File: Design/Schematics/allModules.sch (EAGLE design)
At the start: 152 parts, among them IC1 MAX7219CNG, IC2 MAX7219CNG, IC3 MAX7219CNG, IC4 MAX7219CNG, SW1 arcade_btn, SW2 arcade_btn, SW3 arcade_btn, SW4 arcade_btn, U1 328P, U2 328P, U3 328P, U4 328P, U5 328P, U6 328P

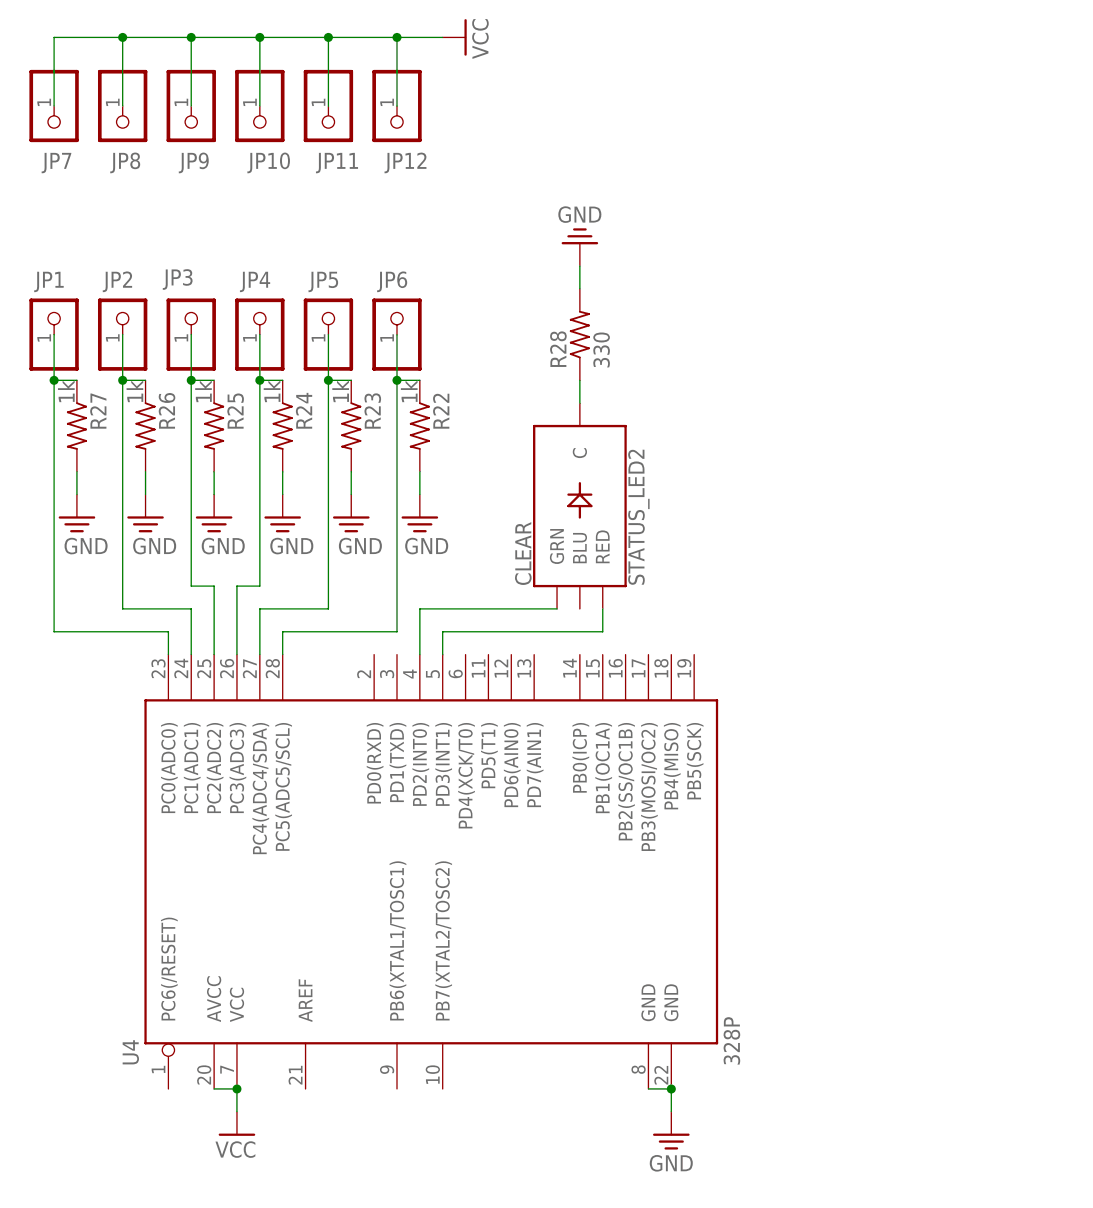
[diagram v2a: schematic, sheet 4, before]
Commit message: Added debug headers and module interconnections
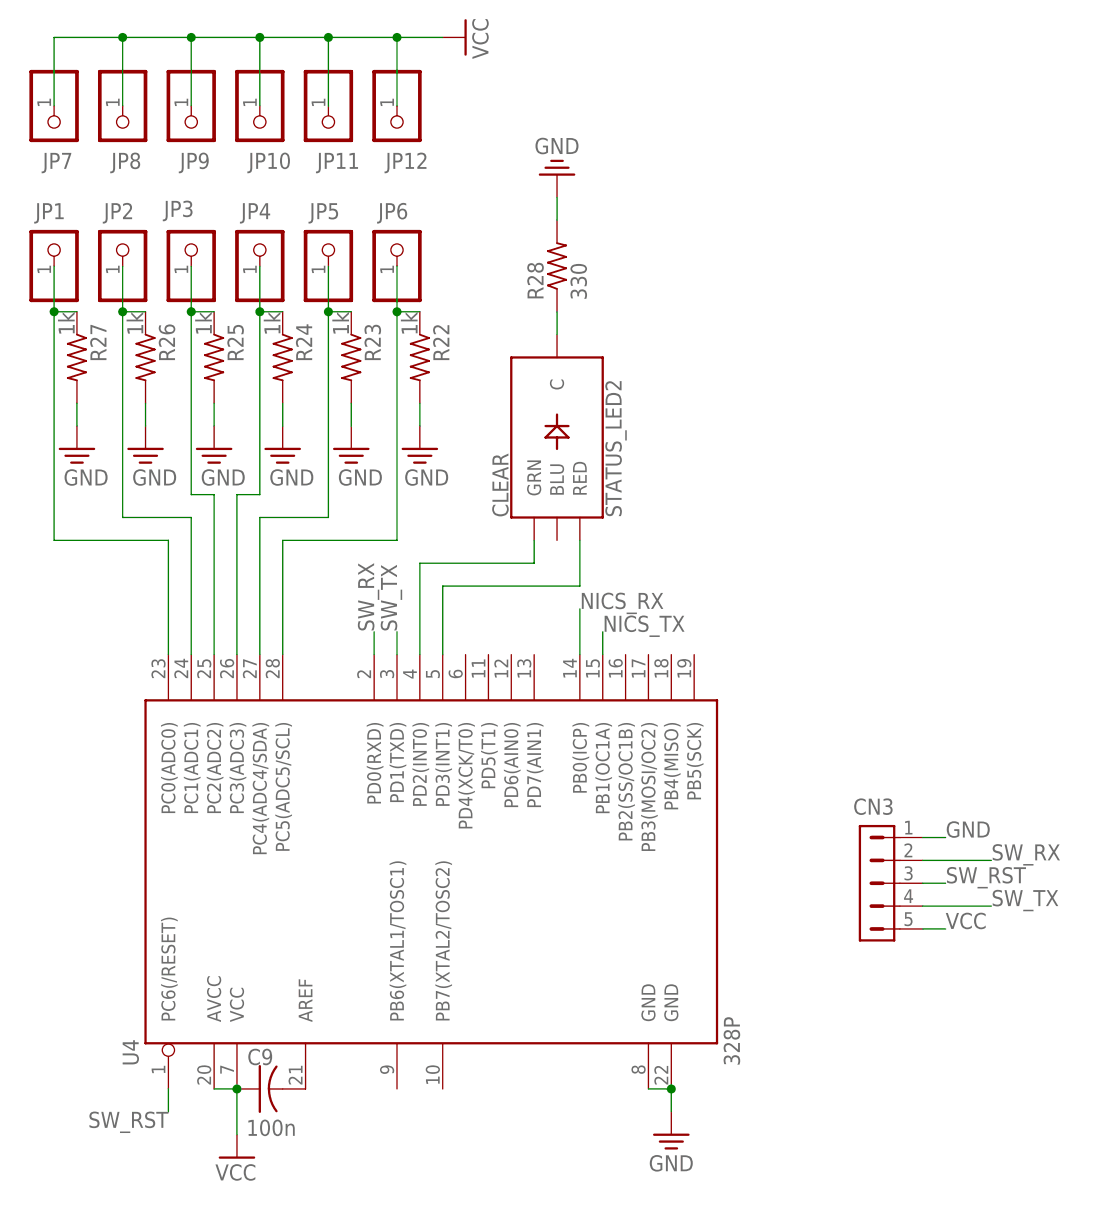
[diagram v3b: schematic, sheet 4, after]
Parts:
- removed SV1: (no value), con-lstb:MA04-1
- added C10, C11, C12, C7, C8, C9: 100n, adafruit:C-US025-024X044
- added CN1, CN2, CN3, CN4, CN5, CN6: (no value), con-hdrs40:HDR-1X5-SIP-100
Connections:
- removed net N$32: SV1.3, U1.PC5(ADC5/SCL)
- removed net N$33: SV1.2, U1.PC4(ADC4/SDA)
- new net BTN_RST: CN2.3, U5.PC6(/RESET)
- new net BTN_RX: CN2.2, U5.PD0(RXD)
- new net BTN_TX: CN2.4, U5.PD1(TXD)
- new net MAI_RST: CN6.3, U1.PC6(/RESET)
- new net MAI_RX: CN6.2, U1.PD0(RXD)
- new net MAI_TX: CN6.4, U1.PD1(TXD)
- new net MEM_RST: CN1.3, U6.PC6(/RESET)
- new net MEM_RX: CN1.2, U6.PD0(RXD)
- new net MEM_TX: CN1.4, U6.PD1(TXD)
- new net MZE_RST: CN4.3, U3.PC6(/RESET)
- new net MZE_RX: CN4.2, U3.PD0(RXD)
- new net MZE_TX: CN4.4, U3.PD1(TXD)
- new net N$107: C7.2, U6.AREF
- new net N$109: C8.2, U5.AREF
- new net N$124: C9.2, U4.AREF
- new net N$138: C10.2, U3.AREF
- new net N$139: C11.2, U2.AREF
- new net N$140: C12.2, U1.AREF
- new net NICS_RX: U1.PB0(ICP), U2.PB0(ICP), U3.PB0(ICP), U4.PB0(ICP), U5.PB0(ICP), U6.PB0(ICP)
- new net NICS_TX: U1.PB1(OC1A), U2.PB1(OC1A), U3.PB1(OC1A), U4.PB1(OC1A), U5.PB1(OC1A), U6.PB1(OC1A)
- new net SAY_RST: CN5.3, U2.PC6(/RESET)
- new net SAY_RX: CN5.2, U2.PD0(RXD)
- new net SAY_TX: CN5.4, U2.PD1(TXD)
- new net SW_RST: CN3.3, U4.PC6(/RESET)
- new net SW_RX: CN3.2, U4.PD0(RXD)
- new net SW_TX: CN3.4, U4.PD1(TXD)
- net GND: now also CN1.1, CN2.1, CN3.1, CN4.1, CN5.1, CN6.1, U1.GND@1, U2.GND@1, U2.GND@2, U5.GND@1, U6.GND@1; no longer SV1.1
- net VCC: now also C10.1, C11.1, C12.1, C7.1, C8.1, C9.1, CN1.5, CN2.5, CN3.5, CN4.5, CN5.5, CN6.5; no longer SV1.4
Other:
- moved on the sheet: JP1, JP2, JP3, JP4, JP5, JP6, R10, R11, R12, R13, R22, R23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

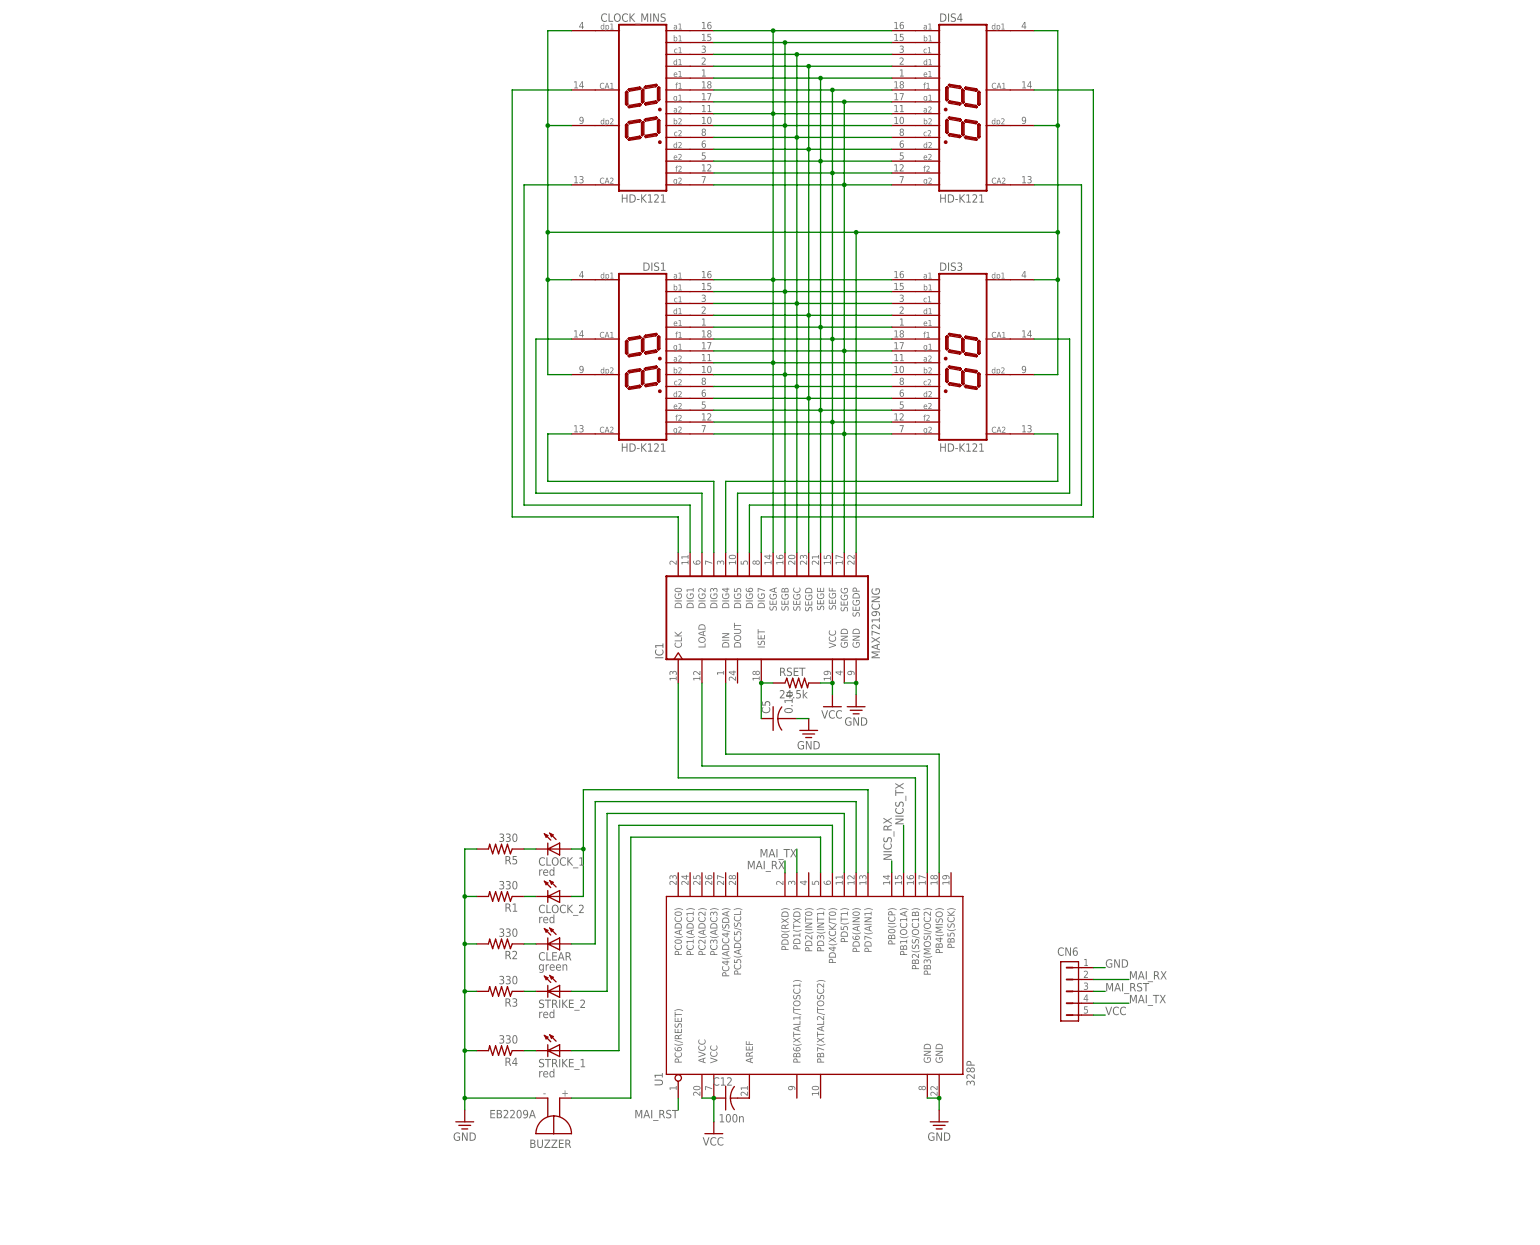
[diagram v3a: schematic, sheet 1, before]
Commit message: Added frames to all modules
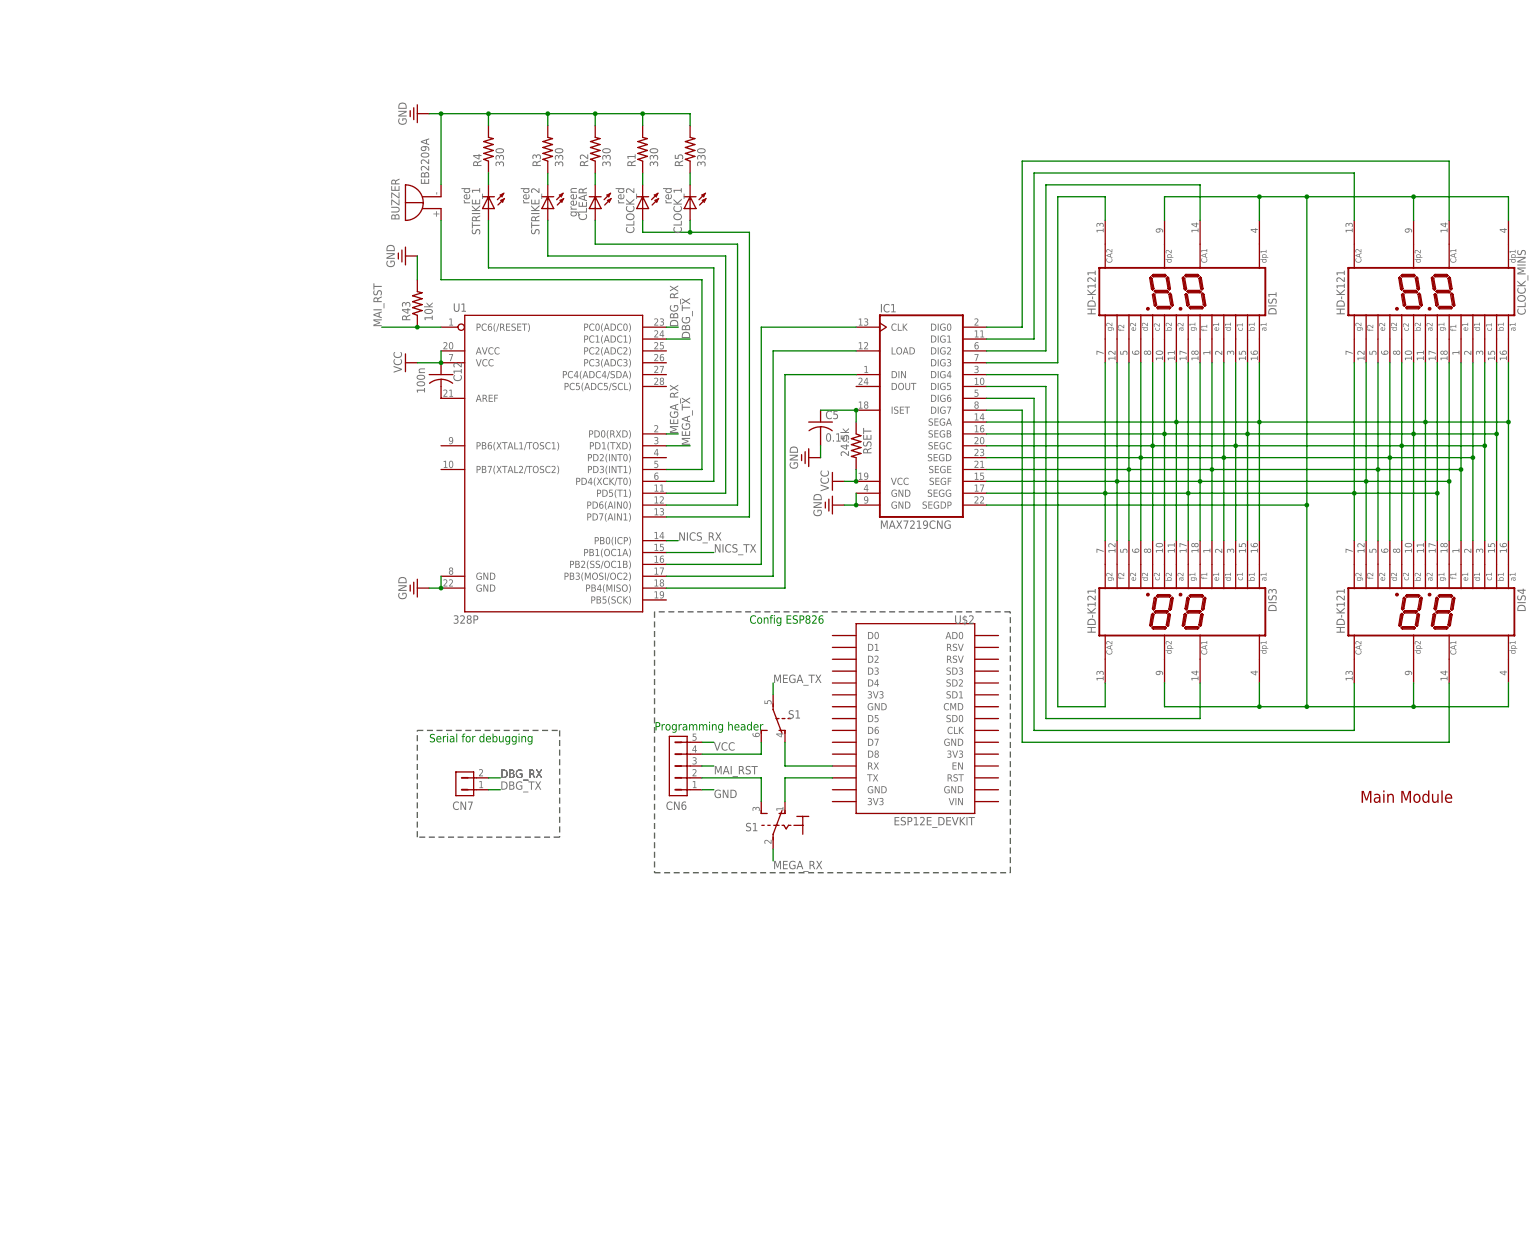
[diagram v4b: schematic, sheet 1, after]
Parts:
- added CN7: (no value), con-hdrs40:HDR-1X2-MTA-100
- added R43, R44, R45, R46, R47, R48: 10k, adafruit:R-US_0309/12
- added S1: (no value), switch:320-938
- added U$2: ESP12E_DEVKIT, ESP12E_DEVKIT:ESP12E_DEVKIT
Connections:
- removed net MAI_RX: CN6.2, U1.PD0(RXD)
- removed net MAI_TX: CN6.4, U1.PD1(TXD)
- new net DBG_RX: CN7.2, U1.PC0(ADC0)
- new net DBG_TX: CN7.1, U1.PC1(ADC1)
- new net MEGA_RX: S11.P, U1.PD0(RXD)
- new net MEGA_TX: S1B.P, U1.PD1(TXD)
- new net N$141: CN6.4, S1B.S
- new net N$142: CN6.2, S11.S
- new net N$32: S11.O, U$2.TX
- new net N$33: S1B.O, U$2.RX
- net BTN_RST: now also R47.1
- net GND: now also R43.2, R44.2, R45.2, R46.2, R47.2, R48.2
- net MAI_RST: now also R43.1
- net MEM_RST: now also R48.1
- net MZE_RST: now also R45.1
- net SAY_RST: now also R44.1
- net SW_RST: now also R46.1
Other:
- note added: "Button Module"
- note added: "Config ESP826"
- note added: "Main Module"
- note added: "Maze Module"
- note added: "Memory Module"
- note added: "Programming header"
- note added: "Serial for debugging"
- note added: "Simon Says Module"
- note added: "Simple Wires Module"
- moved on the sheet: BIG_NUM, BUZZER, C12, C3, C5, C7, CHAR1, CHAR2, CHAR3, CHAR4, CLEAR, CLOCK_1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

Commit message: Revert "Added frames to all modules"
This reverts commit 3eabf43de3682e49b345895a8346113ada920e34
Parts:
- removed CN7: (no value), con-hdrs40:HDR-1X2-MTA-100
- removed R43, R44, R45, R46, R47, R48: 10k, adafruit:R-US_0309/12
- removed S1: (no value), switch:320-938
- removed U$2: ESP12E_DEVKIT, ESP12E_DEVKIT:ESP12E_DEVKIT
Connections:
- removed net DBG_RX: CN7.2, U1.PC0(ADC0)
- removed net DBG_TX: CN7.1, U1.PC1(ADC1)
- removed net MEGA_RX: S11.P, U1.PD0(RXD)
- removed net MEGA_TX: S1B.P, U1.PD1(TXD)
- removed net N$141: CN6.4, S1B.S
- removed net N$142: CN6.2, S11.S
- removed net N$32: S11.O, U$2.TX
- removed net N$33: S1B.O, U$2.RX
- new net MAI_RX: CN6.2, U1.PD0(RXD)
- new net MAI_TX: CN6.4, U1.PD1(TXD)
- net BTN_RST: no longer R47.1
- net GND: no longer R43.2, R44.2, R45.2, R46.2, R47.2, R48.2
- net MAI_RST: no longer R43.1
- net MEM_RST: no longer R48.1
- net MZE_RST: no longer R45.1
- net SAY_RST: no longer R44.1
- net SW_RST: no longer R46.1
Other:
- note removed: "Button Module"
- note removed: "Config ESP826"
- note removed: "Main Module"
- note removed: "Maze Module"
- note removed: "Memory Module"
- note removed: "Programming header"
- note removed: "Serial for debugging"
- note removed: "Simon Says Module"
- note removed: "Simple Wires Module"
- moved on the sheet: BIG_NUM, BUZZER, C12, C3, C5, C7, CHAR1, CHAR2, CHAR3, CHAR4, CLEAR, CLOCK_1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
